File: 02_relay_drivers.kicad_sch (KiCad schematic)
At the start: 68 parts, among them Q1 2N7002K, Q10 2N7002K, Q11 2N7002K, Q12 2N7002K, Q13 2N7002K, Q14 2N7002K, Q15 2N7002K, Q16 2N7002K, Q17 2N7002K, Q2 2N7002K, Q3 2N7002K, Q4 2N7002K, Q5 2N7002K, Q6 2N7002K, Q7 2N7002K, Q8 2N7002K, Q9 2N7002K

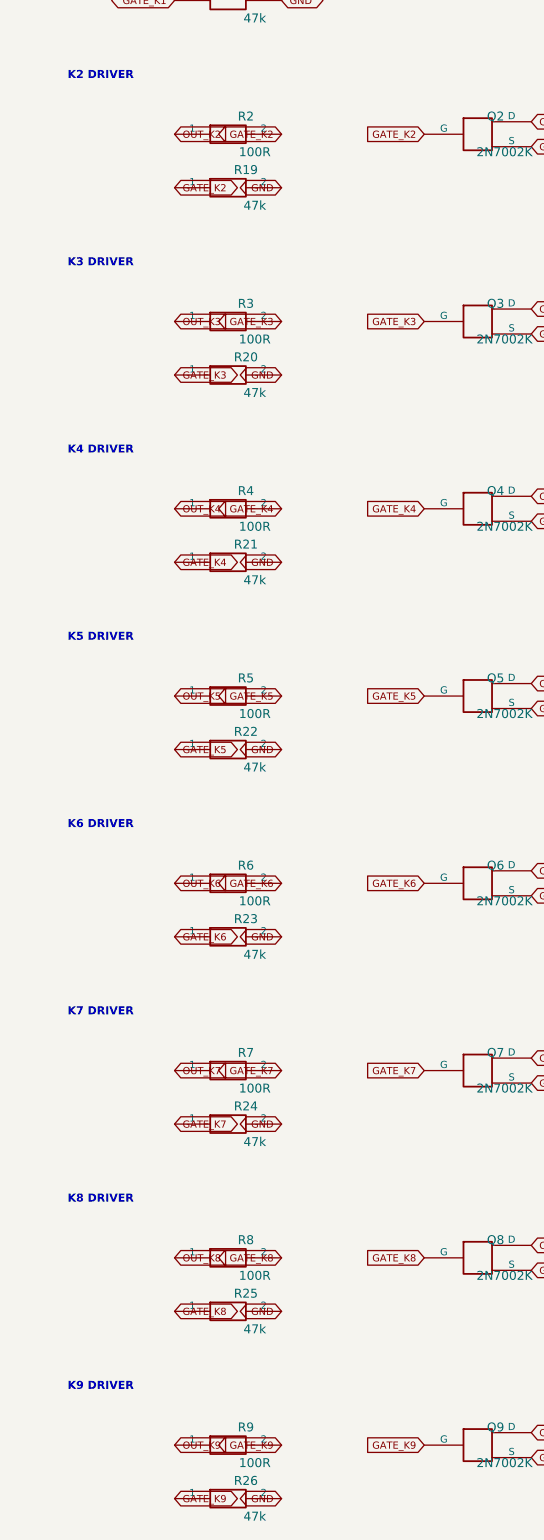
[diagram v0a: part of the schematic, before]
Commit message: Add Phoenix 1190370 connector footprint
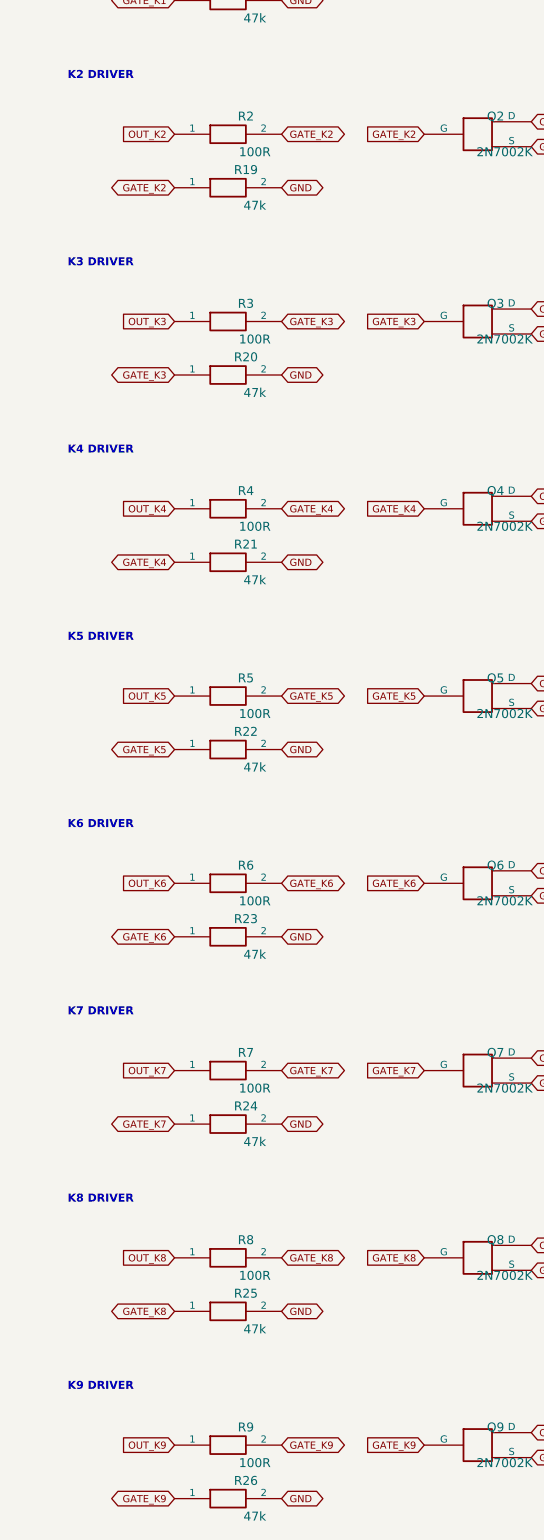
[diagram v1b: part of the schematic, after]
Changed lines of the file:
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@@
 	(global_label "GATE_K8"
 		(shape bidirectional)
-		(at 38.1 223.52 0)
+		(at 38.1 223.52 180)
 		(effects
 			(font
 				(size 1.016 1.016)
 			)
-			(justify left)
+			(justify right)
 		)
 		(property "Intersheetrefs" "${INTERSHEET_REFS}"
@@
 	(global_label "GATE_K3"
 		(shape bidirectional)
-		(at 38.1 90.17 0)
+		(at 38.1 90.17 180)
 		(effects
 			(font
 				(size 1.016 1.016)
 			)
-			(justify left)
+			(justify right)
 		)
 		(property "Intersheetrefs" "${INTERSHEET_REFS}"
@@
 	(global_label "OUT_K7"
 		(shape input)
-		(at 38.1 189.23 0)
+		(at 38.1 189.23 180)
 		(effects
 			(font
 				(size 1.016 1.016)
 			)
-			(justify left)
+			(justify right)
 		)
 		(property "Intersheetrefs" "${INTERSHEET_REFS}"
@@
 	(global_label "GATE_K6"
 		(shape bidirectional)
-		(at 38.1 170.18 0)
+		(at 38.1 170.18 180)
 		(effects
 			(font
 				(size 1.016 1.016)
 			)
-			(justify left)
+			(justify right)
 		)
 		(property "Intersheetrefs" "${INTERSHEET_REFS}"
@@
 	(global_label "GATE_K7"
 		(shape bidirectional)
-		(at 38.1 196.85 0)
+		(at 38.1 196.85 180)
 		(effects
 			(font
 				(size 1.016 1.016)
 			)
-			(justify left)
+			(justify right)
 		)
 		(property "Intersheetrefs" "${INTERSHEET_REFS}"
@@
 	(global_label "OUT_K4"
 		(shape input)
-		(at 38.1 109.22 0)
+		(at 38.1 109.22 180)
 		(effects
 			(font
 				(size 1.016 1.016)
 			)
-			(justify left)
+			(justify right)
 		)
 		(property "Intersheetrefs" "${INTERSHEET_REFS}"
@@
 	(global_label "GATE_K5"
 		(shape bidirectional)
-		(at 38.1 143.51 0)
+		(at 38.1 143.51 180)
 		(effects
 			(font
 				(size 1.016 1.016)
 			)
-			(justify left)
+			(justify right)
 		)
 		(property "Intersheetrefs" "${INTERSHEET_REFS}"
@@
 	(global_label "OUT_K5"
 		(shape input)
-		(at 38.1 135.89 0)
+		(at 38.1 135.89 180)
 		(effects
 			(font
 				(size 1.016 1.016)
 			)
-			(justify left)
+			(justify right)
 		)
 		(property "Intersheetrefs" "${INTERSHEET_REFS}"
@@
 	(global_label "GATE_K4"
 		(shape bidirectional)
-		(at 38.1 116.84 0)
+		(at 38.1 116.84 180)
 		(effects
 			(font
 				(size 1.016 1.016)
 			)
-			(justify left)
+			(justify right)
 		)
 		(property "Intersheetrefs" "${INTERSHEET_REFS}"
@@
 	(global_label "GATE_K6"
 		(shape bidirectional)
-		(at 53.34 162.56 180)
+		(at 53.34 162.56 0)
 		(effects
 			(font
 				(size 1.016 1.016)
 			)
-			(justify right)
+			(justify left)
 		)
 		(property "Intersheetrefs" "${INTERSHEET_REFS}"
@@
 	(global_label "GND"
 		(shape bidirectional)
-		(at 53.34 196.85 180)
+		(at 53.34 196.85 0)
 		(effects
 			(font
 				(size 1.016 1.016)
 			)
-			(justify right)
+			(justify left)
 		)
 		(property "Intersheetrefs" "${INTERSHEET_REFS}"
@@
 	(global_label "GATE_K7"
 		(shape bidirectional)
-		(at 53.34 189.23 180)
+		(at 53.34 189.23 0)
 		(effects
 			(font
 				(size 1.016 1.016)
 			)
-			(justify right)
+			(justify left)
 		)
 		(property "Intersheetrefs" "${INTERSHEET_REFS}"
@@
 	(global_label "OUT_K6"
 		(shape input)
-		(at 38.1 162.56 0)
+		(at 38.1 162.56 180)
 		(effects
 			(font
 				(size 1.016 1.016)
 			)
-			(justify left)
+			(justify right)
 		)
 		(property "Intersheetrefs" "${INTERSHEET_REFS}"
@@
 	(global_label "GATE_K3"
 		(shape bidirectional)
-		(at 53.34 82.55 180)
+		(at 53.34 82.55 0)
 		(effects
 			(font
 				(size 1.016 1.016)
 			)
-			(justify right)
+			(justify left)
 		)
 		(property "Intersheetrefs" "${INTERSHEET_REFS}"
@@
 	(global_label "GND"
 		(shape bidirectional)
-		(at 53.34 170.18 180)
+		(at 53.34 170.18 0)
 		(effects
 			(font
 				(size 1.016 1.016)
 			)
-			(justify right)
+			(justify left)
 		)
 		(property "Intersheetrefs" "${INTERSHEET_REFS}"
@@
 	(global_label "OUT_K8"
 		(shape input)
-		(at 38.1 215.9 0)
+		(at 38.1 215.9 180)
 		(effects
 			(font
 				(size 1.016 1.016)
 			)
-			(justify left)
+			(justify right)
 		)
 		(property "Intersheetrefs" "${INTERSHEET_REFS}"
@@
 	(global_label "GATE_K8"
 		(shape bidirectional)
-		(at 53.34 215.9 180)
+		(at 53.34 215.9 0)
 		(effects
 			(font
 				(size 1.016 1.016)
 			)
-			(justify right)
+			(justify left)
 		)
 		(property "Intersheetrefs" "${INTERSHEET_REFS}"
@@
 	(global_label "GATE_K4"
 		(shape bidirectional)
-		(at 53.34 109.22 180)
+		(at 53.34 109.22 0)
 		(effects
 			(font
 				(size 1.016 1.016)
 			)
-			(justify right)
+			(justify left)
 		)
 		(property "Intersheetrefs" "${INTERSHEET_REFS}"
@@
 	(global_label "GND"
 		(shape bidirectional)
-		(at 53.34 223.52 180)
+		(at 53.34 223.52 0)
 		(effects
 			(font
 				(size 1.016 1.016)
 			)
-			(justify right)
+			(justify left)
 		)
 		(property "Intersheetrefs" "${INTERSHEET_REFS}"
@@
 	(global_label "GATE_K9"
 		(shape bidirectional)
-		(at 38.1 250.19 0)
+		(at 38.1 250.19 180)
 		(effects
 			(font
 				(size 1.016 1.016)
 			)
-			(justify left)
+			(justify right)
 		)
 		(property "Intersheetrefs" "${INTERSHEET_REFS}"
@@
 	(global_label "GND"
 		(shape bidirectional)
-		(at 53.34 63.5 180)
+		(at 53.34 63.5 0)
 		(effects
 			(font
 				(size 1.016 1.016)
 			)
-			(justify right)
+			(justify left)
 		)
 		(property "Intersheetrefs" "${INTERSHEET_REFS}"
@@
 	(global_label "GND"
 		(shape bidirectional)
-		(at 53.34 143.51 180)
+		(at 53.34 143.51 0)
 		(effects
 			(font
 				(size 1.016 1.016)
 			)
-			(justify right)
+			(justify left)
 		)
 		(property "Intersheetrefs" "${INTERSHEET_REFS}"
@@
 	(global_label "GATE_K2"
 		(shape bidirectional)
-		(at 53.34 55.88 180)
+		(at 53.34 55.88 0)
 		(effects
 			(font
 				(size 1.016 1.016)
 			)
-			(justify right)
+			(justify left)
 		)
 		(property "Intersheetrefs" "${INTERSHEET_REFS}"
@@
 	(global_label "OUT_K3"
 		(shape input)
-		(at 38.1 82.55 0)
+		(at 38.1 82.55 180)
 		(effects
 			(font
 				(size 1.016 1.016)
 			)
-			(justify left)
+			(justify right)
 		)
 		(property "Intersheetrefs" "${INTERSHEET_REFS}"
@@
 	(global_label "GND"
 		(shape bidirectional)
-		(at 53.34 116.84 180)
+		(at 53.34 116.84 0)
 		(effects
 			(font
 				(size 1.016 1.016)
 			)
-			(justify right)
+			(justify left)
 		)
 		(property "Intersheetrefs" "${INTERSHEET_REFS}"
@@
 	(global_label "GATE_K9"
 		(shape bidirectional)
-		(at 53.34 242.57 180)
+		(at 53.34 242.57 0)
 		(effects
 			(font
 				(size 1.016 1.016)
 			)
-			(justify right)
+			(justify left)
 		)
 		(property "Intersheetrefs" "${INTERSHEET_REFS}"
@@
 	(global_label "OUT_K2"
 		(shape input)
-		(at 38.1 55.88 0)
+		(at 38.1 55.88 180)
 		(effects
 			(font
 				(size 1.016 1.016)
 			)
-			(justify left)
+			(justify right)
 		)
 		(property "Intersheetrefs" "${INTERSHEET_REFS}"
@@
 	(global_label "GATE_K5"
 		(shape bidirectional)
-		(at 53.34 135.89 180)
+		(at 53.34 135.89 0)
 		(effects
 			(font
 				(size 1.016 1.016)
 			)
-			(justify right)
+			(justify left)
 		)
 		(property "Intersheetrefs" "${INTERSHEET_REFS}"
@@
 	(global_label "OUT_K9"
 		(shape input)
-		(at 38.1 242.57 0)
+		(at 38.1 242.57 180)
 		(effects
 			(font
 				(size 1.016 1.016)
 			)
-			(justify left)
+			(justify right)
 		)
 		(property "Intersheetrefs" "${INTERSHEET_REFS}"
@@
 	(global_label "GND"
 		(shape bidirectional)
-		(at 53.34 90.17 180)
+		(at 53.34 90.17 0)
 		(effects
 			(font
 				(size 1.016 1.016)
 			)
-			(justify right)
+			(justify left)
 		)
 		(property "Intersheetrefs" "${INTERSHEET_REFS}"
@@
 	(global_label "GATE_K2"
 		(shape bidirectional)
-		(at 38.1 63.5 0)
+		(at 38.1 63.5 180)
 		(effects
 			(font
 				(size 1.016 1.016)
 			)
-			(justify left)
+			(justify right)
 		)
 		(property "Intersheetrefs" "${INTERSHEET_REFS}"
@@
 	(global_label "GND"
 		(shape bidirectional)
-		(at 53.34 250.19 180)
+		(at 53.34 250.19 0)
 		(effects
 			(font
 				(size 1.016 1.016)
 			)
-			(justify right)
+			(justify left)
 		)
 		(property "Intersheetrefs" "${INTERSHEET_REFS}"
